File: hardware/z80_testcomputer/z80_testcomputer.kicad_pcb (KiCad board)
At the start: 2 copper layers, 95 x 100 mm, 23 parts, among them J1 Conn_02x15_Odd_Even, J2 Conn_02x15_Odd_Even, J3 Conn_01x32, U1 Z84C000XPEG, U2 SRAM_512K8B_DIP_SOP_SOJ, U3 EEPROM_512K8B_DIP, U4 Z84C200XPEG

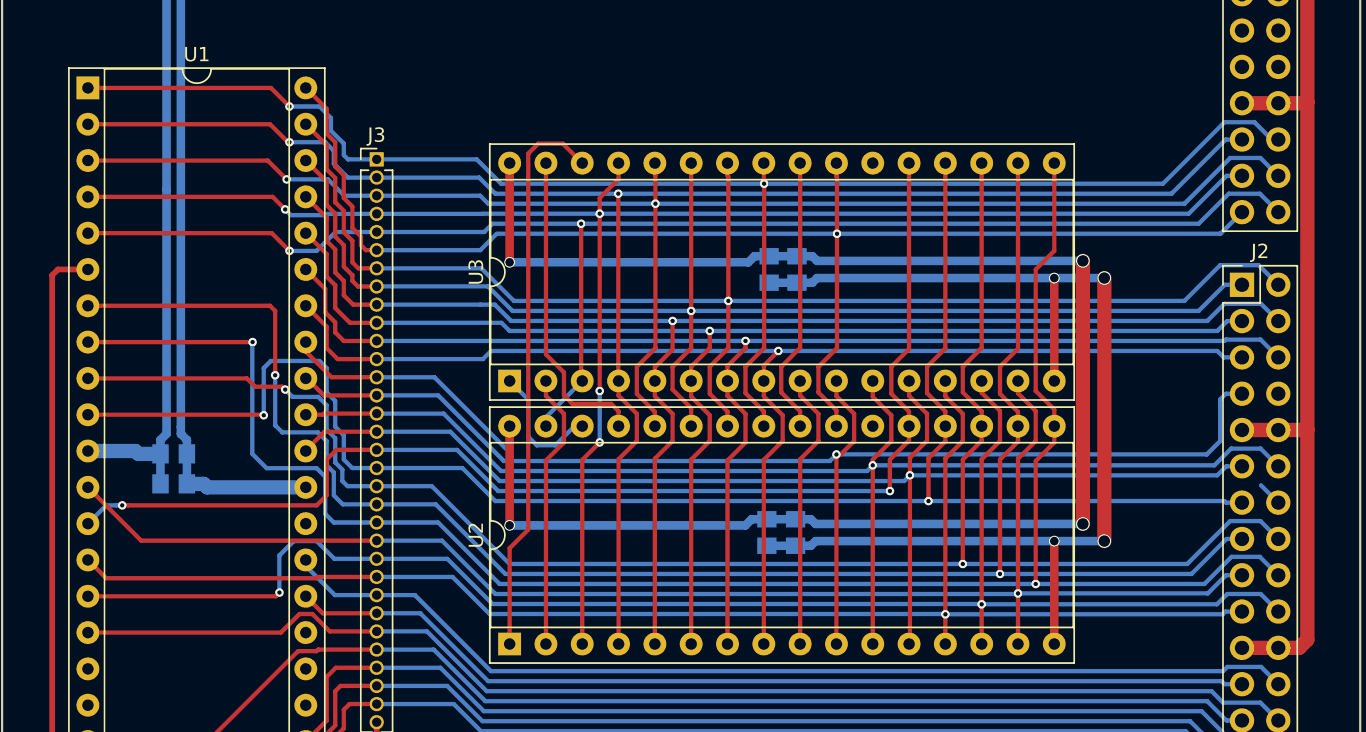
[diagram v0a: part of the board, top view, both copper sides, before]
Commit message: changed address bus ordering, changed peripheral bus to something smaller
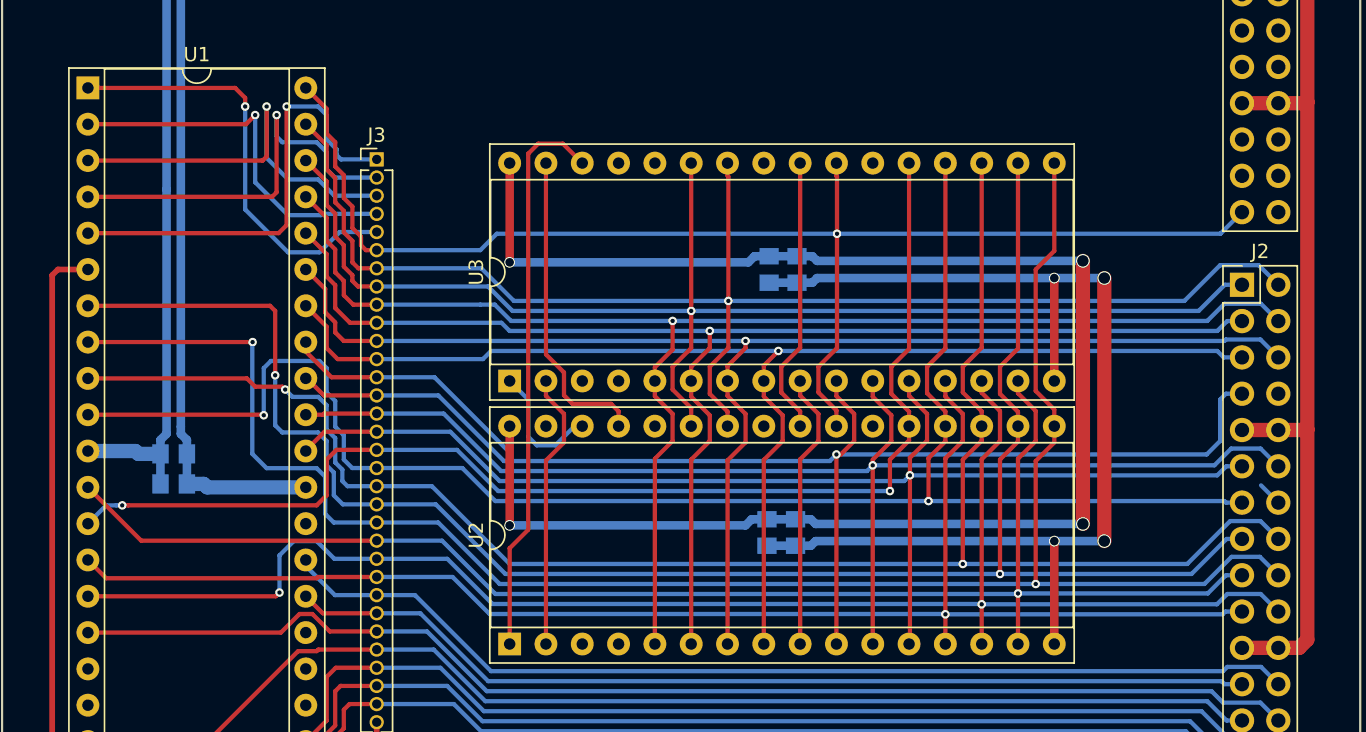
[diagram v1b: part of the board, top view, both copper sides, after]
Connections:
- J3 pad 1: /A11 -> /A15
- J3 pad 2: /A12 -> /A14
- J3 pad 4: /A14 -> /A12
- J3 pad 5: /A15 -> /A11
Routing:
- net /A12: track 117.4 -> 26.2 mm, vias 2 -> 1
- net /A14: track 117.1 -> 29.1 mm, vias 4 -> 1
- net /A11: track 108.8 -> 30.1 mm, vias 2 -> 1
- net /A13: track 105.8 -> 28.5 mm, vias 2 -> 1
- net /A15: track 101.2 -> 31.5 mm, vias 2 -> 1

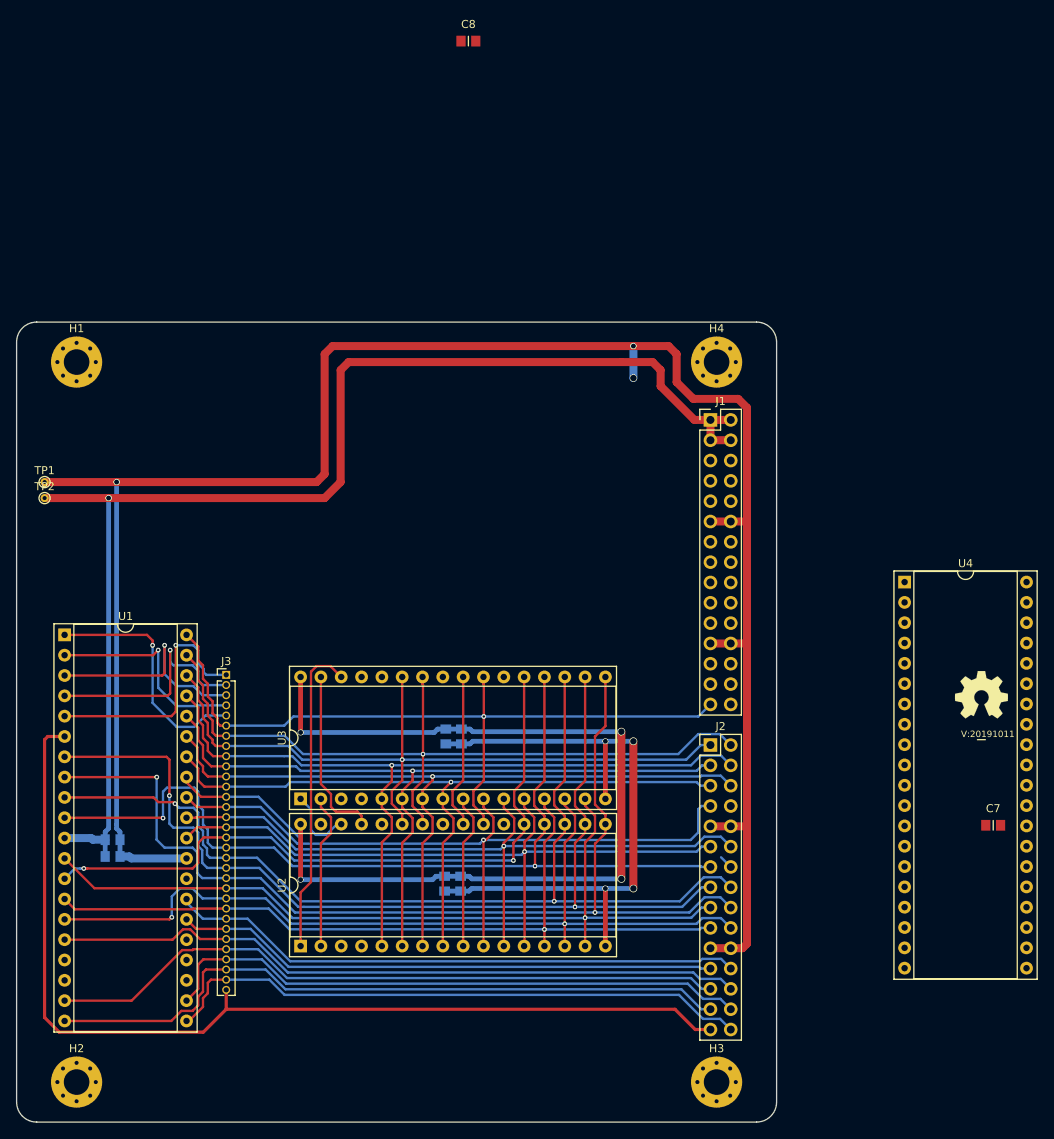
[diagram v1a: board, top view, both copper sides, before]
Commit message: expansion bus changes to make it easier to layout, routed mainboard busses completely
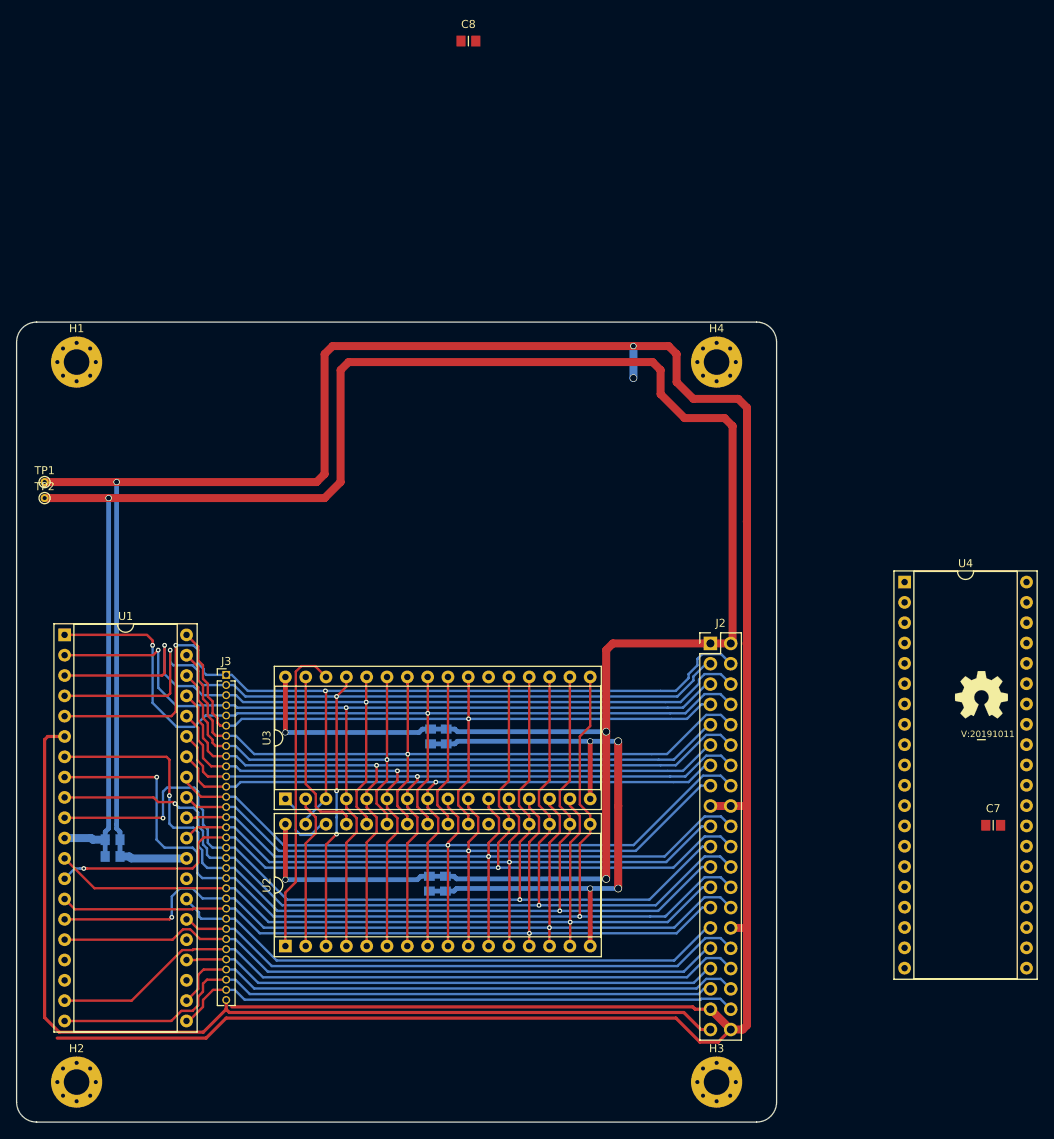
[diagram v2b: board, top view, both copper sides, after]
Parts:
- removed J1: Conn_02x15_Odd_Even, Connector_PinHeader_2.54mm:PinHeader_2x15_P2.54mm_Vertical
- J2: footprint Connector_PinHeader_2.54mm:PinHeader_2x15_P2.54mm_Vertical -> Connector_PinHeader_2.54mm:PinHeader_2x20_P2.54mm_Vertical
- J3: footprint Connector_PinHeader_1.27mm:PinHeader_1x32_P1.27mm_Vertical -> Connector_PinHeader_1.27mm:PinHeader_1x33_P1.27mm_Vertical
- moved J2 12.7 mm to (189.2, 90.2)
- moved C3 1.90 mm to (154.1, 120.2)
- moved C4 1.90 mm to (156.1, 120.2)
- moved C5 1.90 mm to (156.2, 101.8)
- moved C6 1.90 mm to (154.2, 101.8)
- moved U2 1.90 mm to (136.1, 128.0)
- moved U3 1.90 mm to (136.1, 109.6)
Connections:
- J2 pad 1: /A8 -> /VDD
- J2 pad 10: /VSS -> /A9
- J2 pad 11: /A0 -> /A6
- J2 pad 12: /A1 -> /A7
- J2 pad 13: /D6 -> /A4
- J2 pad 14: /D7 -> /A5
- J2 pad 15: /D4 -> /A2
- J2 pad 16: /D5 -> /A3
- J2 pad 17: /D2 -> /VSS
- J2 pad 18: /D3 -> /VSS
- J2 pad 19: /D0 -> /A0
- J2 pad 2: /A9 -> /VDD
- J2 pad 20: /D1 -> /A1
- J2 pad 21: /VSS -> /D6
- J2 pad 22: /VSS -> /D7
- J2 pad 23: /!RESET -> /D4
- J2 pad 24: /!M1 -> /D5
- J2 pad 25: /!MREQ -> /D2
- J2 pad 26: /!INT -> /D3
- J2 pad 27: /!IORQ -> /D0
- J2 pad 28: /!WR -> /D1
- J2 pad 29: /MCLK -> /!M1
- J2 pad 3: /A6 -> /A14
- J2 pad 30: /!RD -> /VSS
- J2 pad 4: /A7 -> /A15
- J2 pad 5: /A4 -> /A12
- J2 pad 6: /A5 -> /A13
- J2 pad 7: /A2 -> /A10
- J2 pad 8: /A3 -> /A11
- J2 pad 9: /VSS -> /A8
- J3 pad 29: /!WR -> /!WAIT
- J3 pad 30: /!IORQ -> /!WR
- J3 pad 31: /!RD -> /!IORQ
- J3 pad 32: /MCLK -> /!RD
- U1 pad 24: (no net) -> /!WAIT
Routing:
- net /VSS: track 333.9 -> 485.4 mm
- net /A14: track 29.1 -> 126.9 mm, vias 1 -> 4
- net /A12: track 26.2 -> 118.9 mm, vias 1 -> 2
- net /A13: track 28.5 -> 113.6 mm, vias 1 -> 2
- net /A15: track 31.5 -> 116.3 mm, vias 1 -> 2
- net /A11: track 30.1 -> 114.3 mm, vias 1 -> 2
- net /!WAIT: track 0.00 -> 67.5 mm
- net /A3: track 37.2 -> 95.5 mm, vias 0 -> 1
- net /VDD: track 273.5 -> 323.0 mm
- net /D7: track 87.1 -> 116.0 mm
- net /D6: track 116.6 -> 125.2 mm
- net /!RESET: track 68.0 -> 72.4 mm
- net /!MREQ: track 85.4 -> 88.9 mm
- net /!RD: track 74.2 -> 71.2 mm
- net /!IORQ: track 87.5 -> 85.1 mm
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
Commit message: started routing PIO chip
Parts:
- moved C7 76.7 mm to (154.7, 81.2), turned to 270 degrees
- moved C8 66.6 mm to (152.8, 81.2), turned to 270 degrees
- moved U4 30.2 mm to (184.3, 74.6), turned to 270 degrees
- moved C3 0.30 mm to (154.1, 119.9)
- moved C4 0.30 mm to (156.1, 119.9)
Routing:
- net /VSS: track 485.4 -> 492.8 mm, vias 7 -> 5
- net /VDD: track 323.0 -> 320.1 mm
- net /D7: track 116.0 -> 114.9 mm

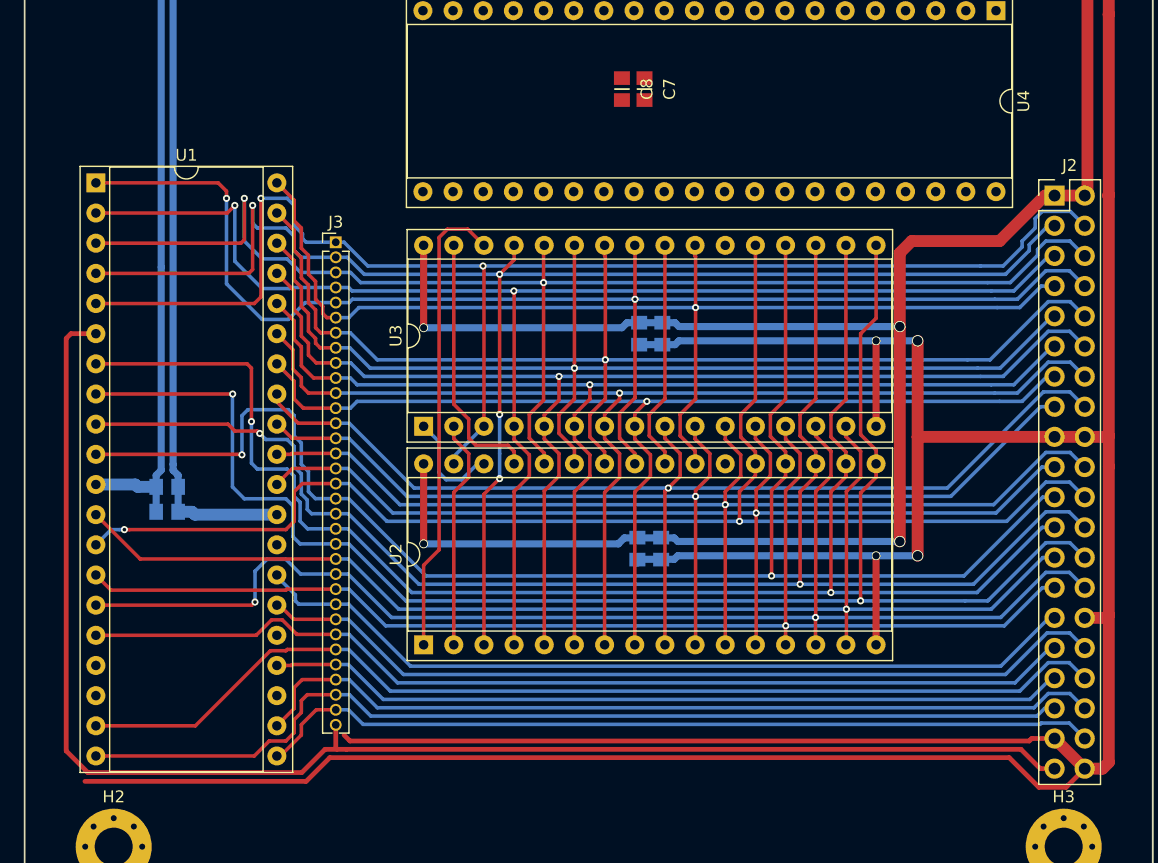
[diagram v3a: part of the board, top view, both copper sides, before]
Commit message: clock rerouted, removed PIO chip
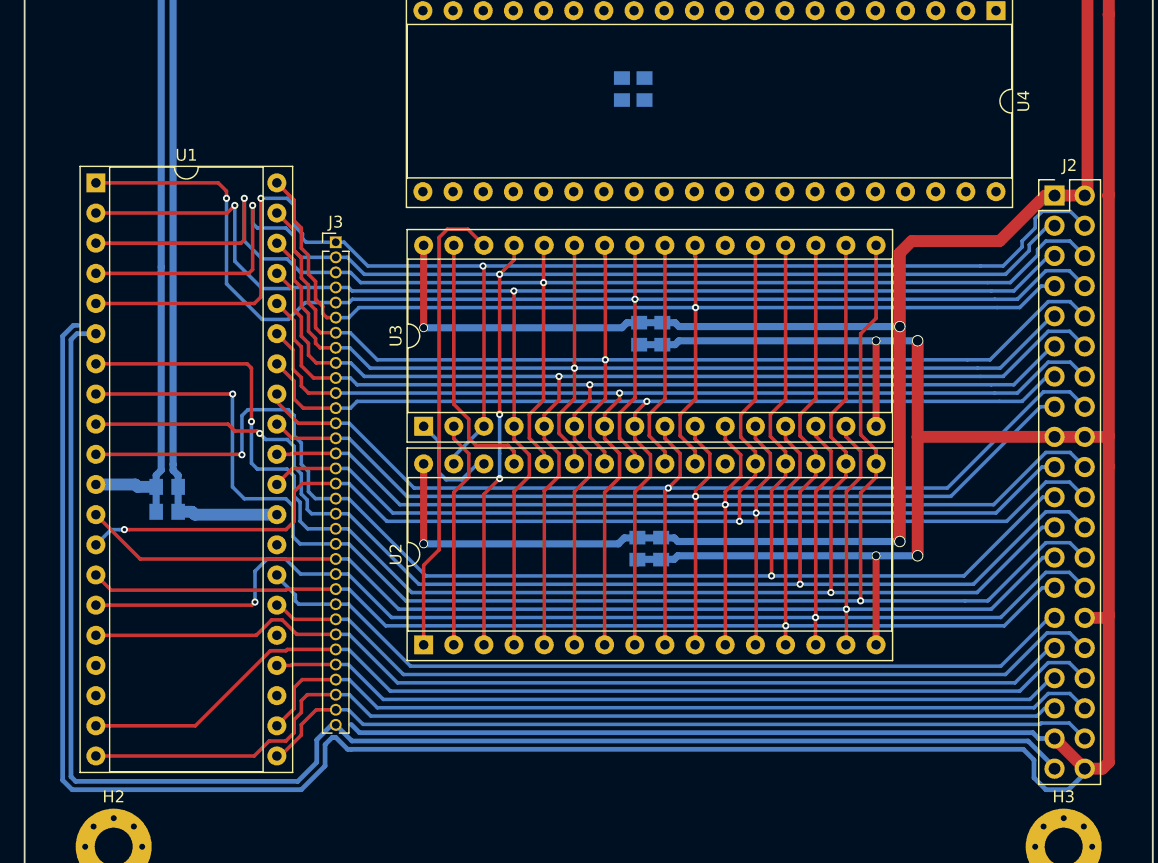
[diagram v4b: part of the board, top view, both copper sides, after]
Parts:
- C7, C8: moved to B.Cu
- turned C7 to 90 degrees
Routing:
- net /VSS: track 492.8 -> 537.7 mm
- net /MCLK: track 125.0 -> 126.8 mm
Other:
- net class CLK: clearance 0.3 -> 0.2

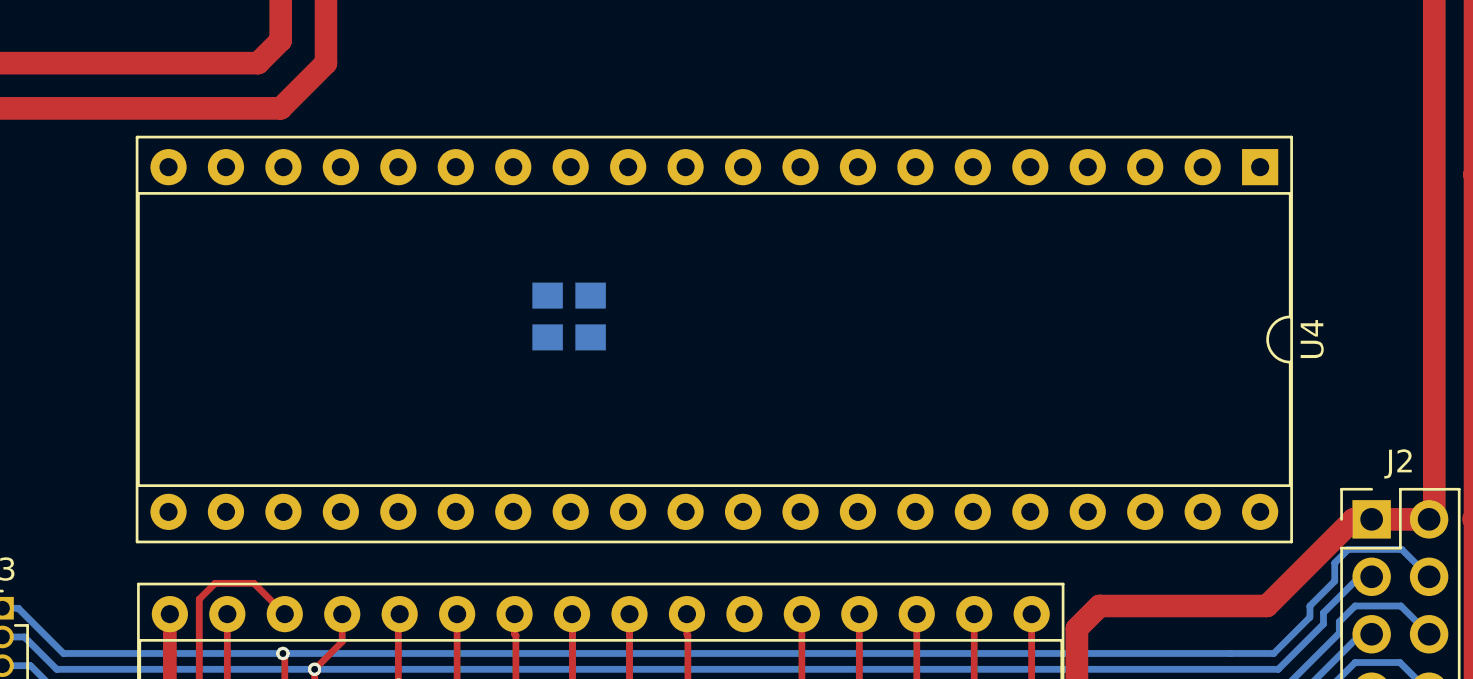
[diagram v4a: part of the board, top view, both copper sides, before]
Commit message: added IO space decoder
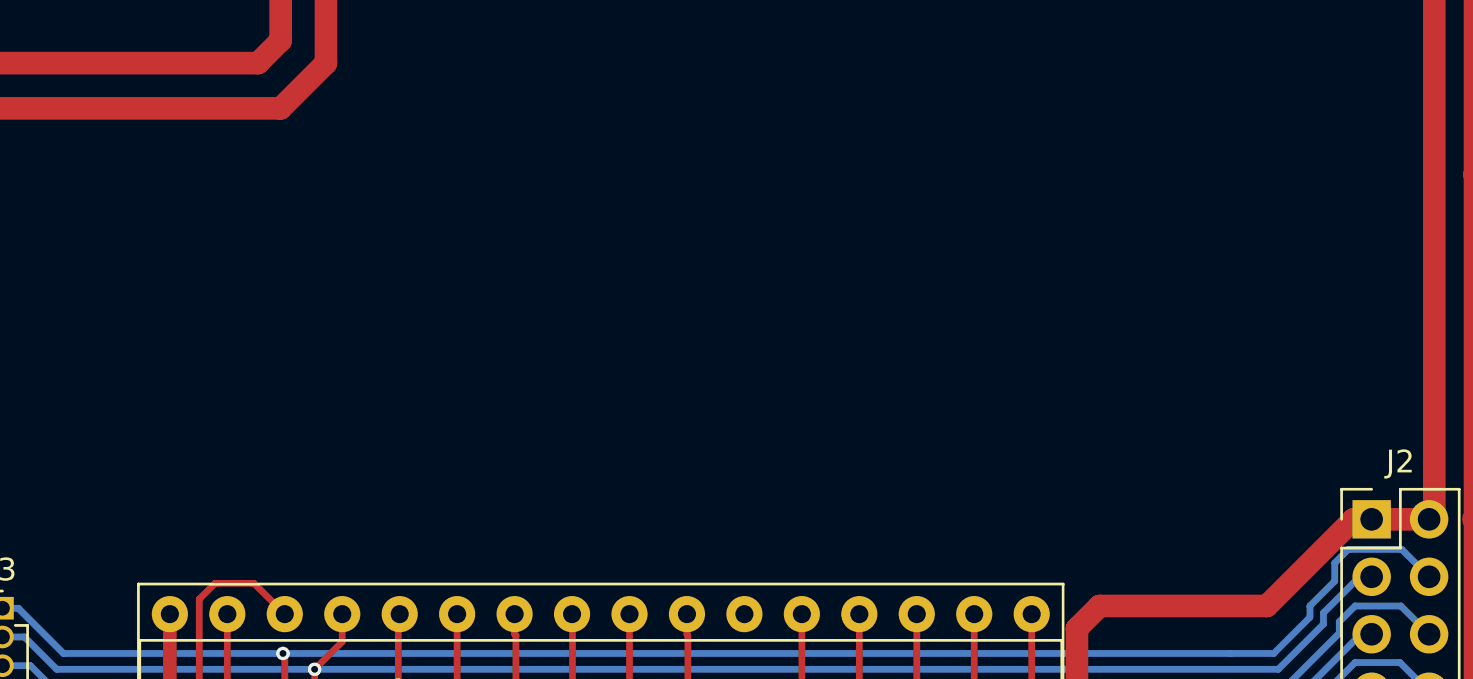
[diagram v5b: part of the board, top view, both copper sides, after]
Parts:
- removed C7: 100n, SquantorRcl:C_0805+0603
- removed C8: 1u, SquantorRcl:C_0805+0603
- removed U4: Z84C200XPEG, Package_DIP:DIP-40_W15.24mm_Socket
